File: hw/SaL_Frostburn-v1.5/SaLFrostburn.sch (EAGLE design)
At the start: 95 parts, among them J1 BAT, U1 ATSAMD21G-A, U2 CC1120, U3 ADXL345, U4 gps, Y1 32.768kHx, Y3 32MHz

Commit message: minor changes to HW
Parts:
- removed J1: BAT, SparkFun-Connectors:JST_2MM_MALE
- added JP5: (no value), SparkFun-Connectors:M024UCON-15767
- added STANDOFF4: STAND-OFF, SparkFun-Electromechanical:STAND-OFF
- added U$7: ADXL193, SparkFun-Sensors:ADXL193
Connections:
- net GND: now also JP5.1; no longer J1.-
- net RAW: now also JP5.2; no longer J1.+
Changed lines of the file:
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@@
 <part name="GND3" library="SparkFun-Aesthetics" deviceset="GND" device=""/>
 <part name="U$3" library="SaL-lib" deviceset="SI7615ADN" device=""/>
-<part name="J1" library="SparkFun-Connectors" deviceset="JST_2MM_MALE" device="" value="BAT"/>
 <part name="GND4" library="SparkFun-Aesthetics" deviceset="GND" device=""/>
 <part name="L1" library="SparkFun-Passives" deviceset="INDUCTOR" device="0603" value="FB - 30Ohm"/>
@@
 <part name="U$4" library="SaL-lib1" deviceset="SIS410DN" device=""/>
 <part name="U$6" library="SaL-lib1" deviceset="SIS410DN" device=""/>
+<part name="JP5" library="SparkFun-Connectors" deviceset="M02" device="4UCON-15767"/>
+<part name="STANDOFF4" library="SparkFun-Electromechanical" deviceset="STAND-OFF" device=""/>
+<part name="U$7" library="SparkFun-Sensors" deviceset="ADXL193" device=""/>
 </parts>
 <sheets>
@@
 <instance part="GND3" gate="1" x="27.94" y="254"/>
 <instance part="U$3" gate="G$1" x="43.18" y="259.08"/>
-<instance part="J1" gate="G$1" x="10.16" y="269.24" rot="R90"/>
 <instance part="GND4" gate="1" x="17.78" y="266.7"/>
 <instance part="L1" gate="G$1" x="109.22" y="205.74" smashed="yes">
@@
 <instance part="U$4" gate="G$1" x="91.44" y="76.2"/>
 <instance part="U$6" gate="G$1" x="96.52" y="35.56"/>
+<instance part="JP5" gate="G$1" x="7.62" y="269.24"/>
+<instance part="STANDOFF4" gate="G$1" x="271.78" y="106.68"/>
+<instance part="U$7" gate="G$1" x="83.82" y="119.38"/>
 </instances>
 <busses>
@@
 </segment>
 <segment>
-<pinref part="J1" gate="G$1" pin="-"/>
 <pinref part="GND4" gate="1" pin="GND"/>
 <wire x1="17.78" y1="269.24" x2="15.24" y2="269.24" width="0.1524" layer="91"/>
+<pinref part="JP5" gate="G$1" pin="1"/>
 </segment>
 <segment>
@@
 </segment>
 <segment>
-<pinref part="J1" gate="G$1" pin="+"/>
 <wire x1="15.24" y1="271.78" x2="17.78" y2="271.78" width="0.1524" layer="91"/>
 <label x="17.78" y="271.78" size="1.27" layer="95" xref="yes"/>
-</segment>
-<segment>
+<pinref part="JP5" gate="G$1" pin="2"/>
+</segment>
+<segment>

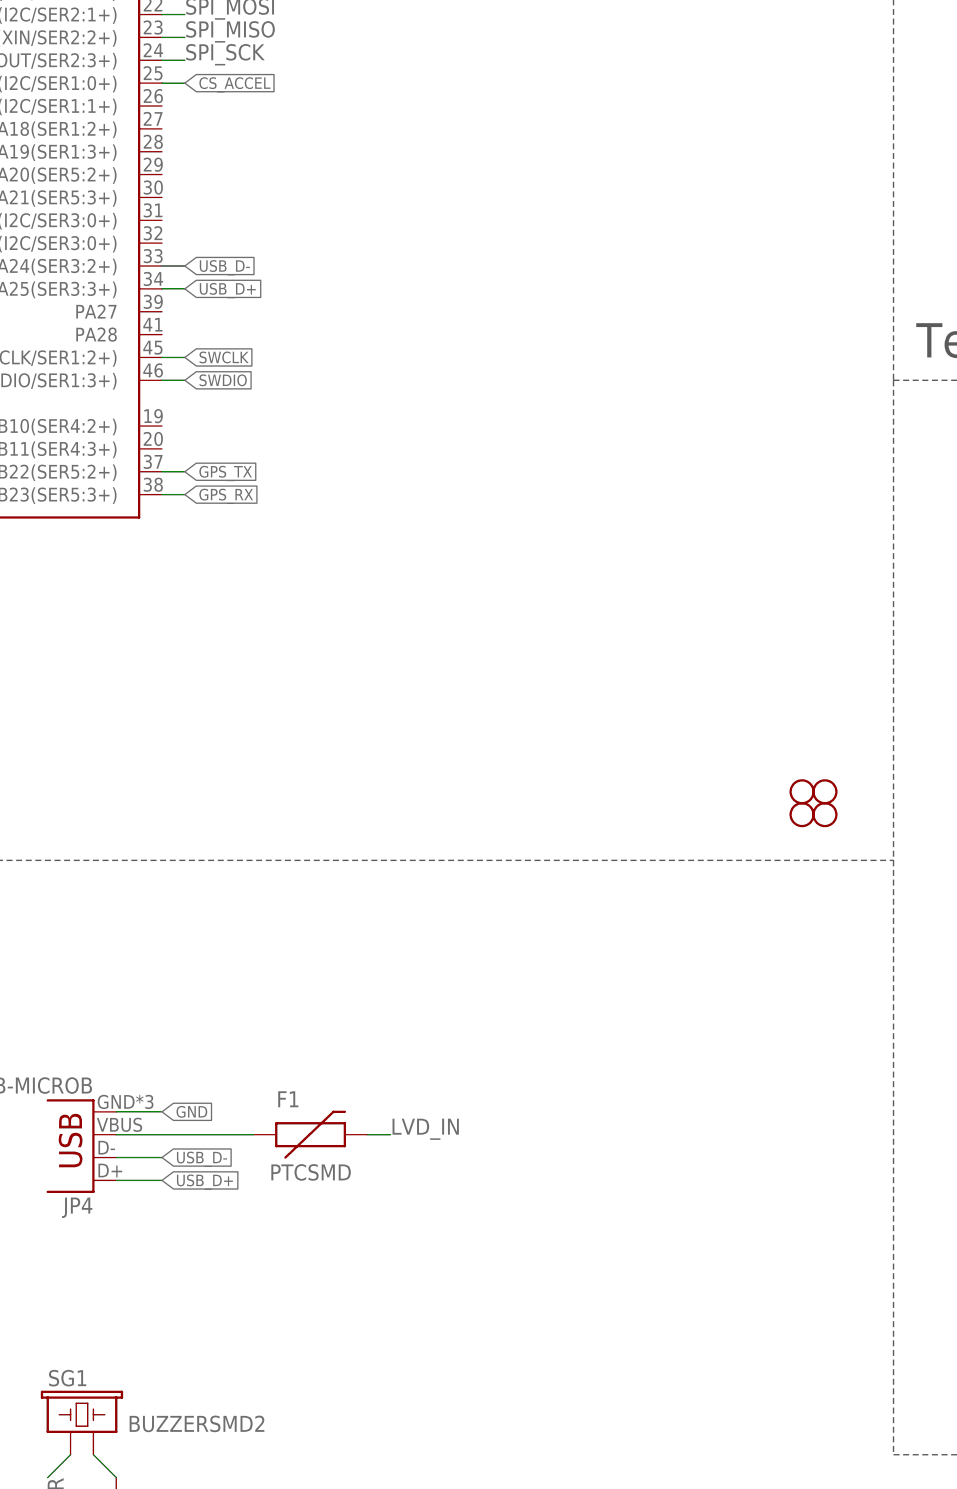
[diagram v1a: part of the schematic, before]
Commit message: minor hardware changes, added led and analog accel
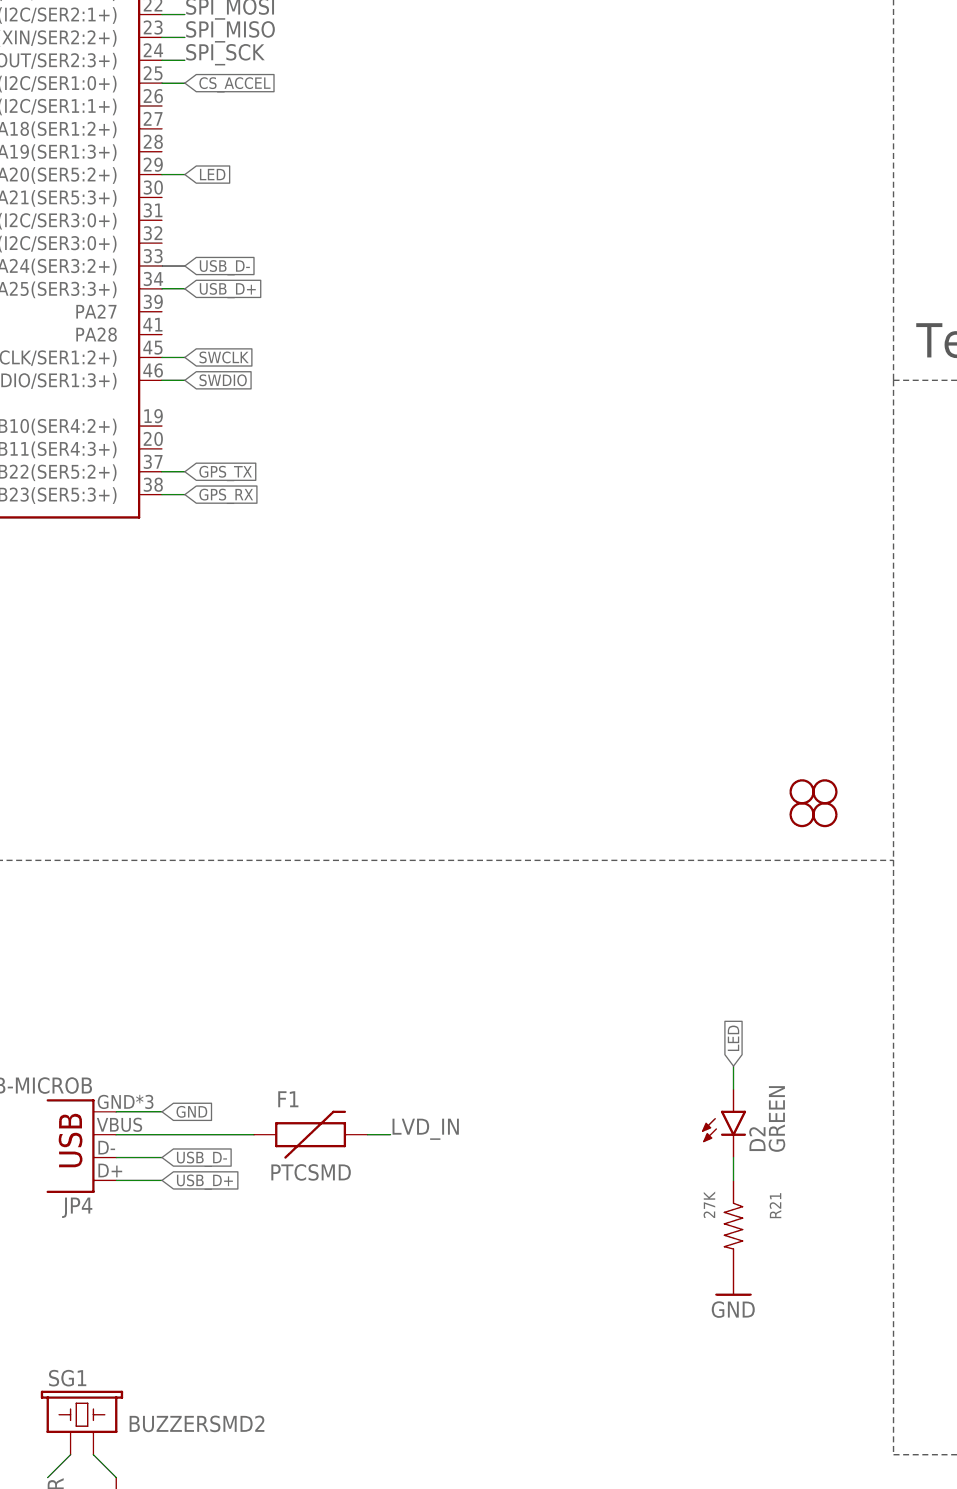
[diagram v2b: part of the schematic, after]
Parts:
- added D2: GREEN, SparkFun-LED:LED-GREEN1206
- added R21: 27K, SparkFun-Resistors:RESISTOR0402
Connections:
- new net LED: D2.A, U1.PA20(SER5:2+)
- new net N$29: D2.C, R21.1
- net GND: now also R21.2
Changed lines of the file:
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@@
 <part name="STANDOFF4" library="SparkFun-Electromechanical" deviceset="STAND-OFF" device=""/>
 <part name="U$7" library="SparkFun-Sensors" deviceset="ADXL193" device=""/>
+<part name="D2" library="SparkFun-LED" deviceset="LED-GREEN" device="1206" value="GREEN"/>
+<part name="R21" library="SparkFun-Resistors" deviceset="RESISTOR" device="0402" value="27K"/>
+<part name="GND51" library="SparkFun-Aesthetics" deviceset="GND" device=""/>
 </parts>
 <sheets>
@@
 <instance part="STANDOFF4" gate="G$1" x="271.78" y="106.68"/>
 <instance part="U$7" gate="G$1" x="83.82" y="119.38"/>
+<instance part="D2" gate="G$1" x="264.16" y="73.66"/>
+<instance part="R21" gate="G$1" x="264.16" y="60.96" smashed="yes" rot="R270">
+<attribute name="NAME" x="268.1986" y="64.77" size="1.27" layer="95" rot="R270"/>
+<attribute name="VALUE" x="260.858" y="64.77" size="1.27" layer="96" rot="R270"/>
+</instance>
+<instance part="GND51" gate="1" x="264.16" y="53.34"/>
 </instances>
 <busses>
@@
 <pinref part="GND50" gate="1" pin="GND"/>
 </segment>
+<segment>
+<pinref part="GND51" gate="1" pin="GND"/>
+<pinref part="R21" gate="G$1" pin="2"/>
+</segment>
 </net>
 <net name="LVD_IN" class="0">
@@
 </segment>
 </net>
+<net name="N$29" class="0">
+<segment>
+<pinref part="D2" gate="G$1" pin="C"/>
+<pinref part="R21" gate="G$1" pin="1"/>
+<wire x1="264.16" y1="66.04" x2="264.16" y2="68.58" width="0.1524" layer="91"/>
+</segment>
+</net>
+<net name="LED" class="0">
+<segment>
+<pinref part="U1" gate="G$1" pin="PA20(SER5:2+)"/>
+<wire x1="200.66" y1="177.8" x2="203.2" y2="177.8" width="0.1524" layer="91"/>
+<label x="203.2" y="177.8" size="1.27" layer="95" xref="yes"/>
+</segment>
+<segment>
+<pinref part="D2" gate="G$1" pin="A"/>
+<wire x1="264.16" y1="76.2" x2="264.16" y2="78.74" width="0.1524" layer="91"/>
+<label x="264.16" y="78.74" size="1.27" layer="95" rot="R90" xref="yes"/>
+</segment>
+</net>
